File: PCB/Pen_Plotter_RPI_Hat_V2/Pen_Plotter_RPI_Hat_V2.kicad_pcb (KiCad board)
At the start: 4 copper layers, 85 x 56 mm, 33 parts, among them J1 RASM712PX, J2 X_LIMIT_SWITCH, J3 X-AXIS_STEPPER, J4 Y_LIMIT_SWITCH, J5 SERVO, J6 Y-AXIS_STEPPER, J7 PAPER_SENSOR, J8 DC_MOTOR, U1 BIDIRECTIONAL_LEVEL_SHIFTER_7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, U2 MINI560, U3 METRO_MINI_2590, U4 X-AXIS_DRV8825_STEPPER_MOTOR_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, U5 Y-AXIS_DRV8825_STEPPER_MOTOR_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, U6 RPI3-MODBP-BULK, U7 LM393AN

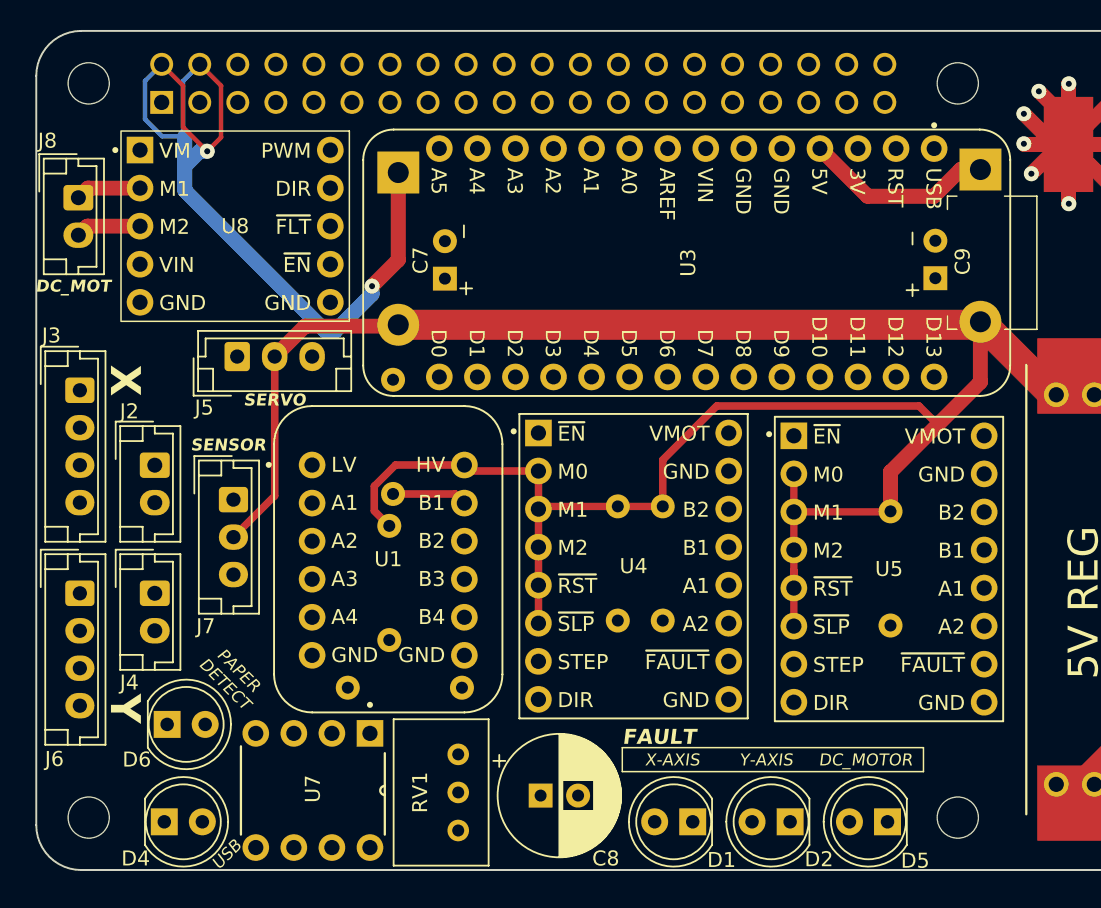
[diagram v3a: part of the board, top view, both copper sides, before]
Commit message: Completed PCB routing, working on resolving final DRC errors
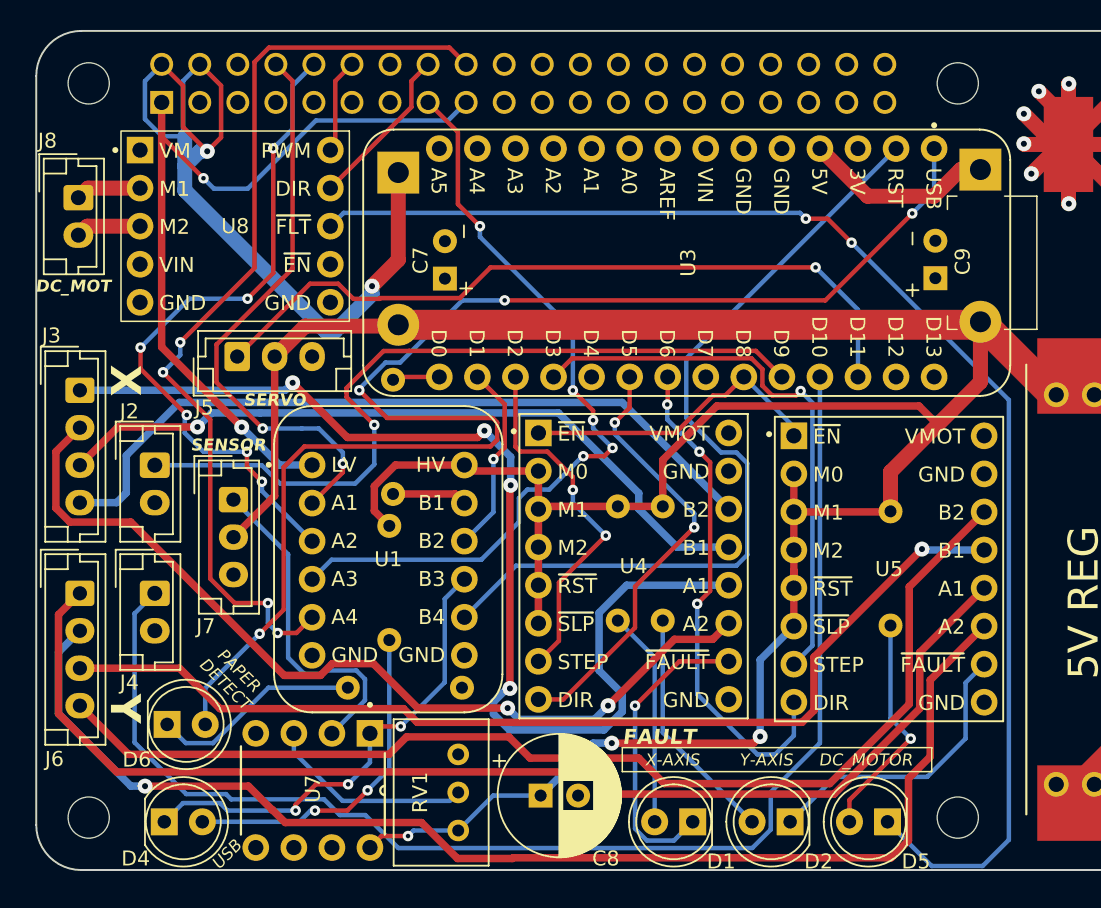
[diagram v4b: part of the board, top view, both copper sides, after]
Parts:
- D1, D2, D5: footprint LED_THT:LED_D5.0mm -> Pen_Plotter_Lib:LED_D5.0mm
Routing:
- net Net-(D6-A): track 0.00 -> 92.4 mm, vias 0 -> 4
- net /Raspberry Pi/DC_MOT_FLT: track 0.00 -> 90.2 mm, vias 0 -> 2
- net Y_LIMIT: track 0.00 -> 88.0 mm
- net /Stepper Motors/Y-AXIS_A2: track 0.00 -> 83.8 mm, vias 0 -> 1
- net /Stepper Motors/Y-AXIS_A1: track 0.00 -> 80.5 mm
- net /Stepper Motors/Y-AXIS_B2: track 0.00 -> 75.6 mm
- net /Stepper Motors/X-AXIS_A1: track 0.00 -> 75.3 mm, vias 0 -> 4
- net /Stepper Motors/Y_AXIS_B1: track 0.00 -> 68.7 mm, vias 0 -> 1
- net MCU_RESET_3V3: track 0.00 -> 62.8 mm, vias 0 -> 4
- net /Stepper Motors/X-AXIS_A2: track 0.00 -> 60.1 mm, vias 0 -> 2
- net +3V3: track 0.00 -> 56.1 mm, vias 0 -> 2
- net MCU_RESET: track 0.00 -> 55.8 mm
- net PAPER_SENSOR_OUT_3V3: track 0.00 -> 52.8 mm, vias 0 -> 5
- net X_LIMIT: track 0.00 -> 52.4 mm, vias 0 -> 1
- net /Stepper Motors/X-AXIS_B2: track 0.00 -> 50.5 mm
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
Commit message: Completed PCB
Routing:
- net /Stepper Motors/Y-AXIS_A2: track 83.8 -> 85.8 mm

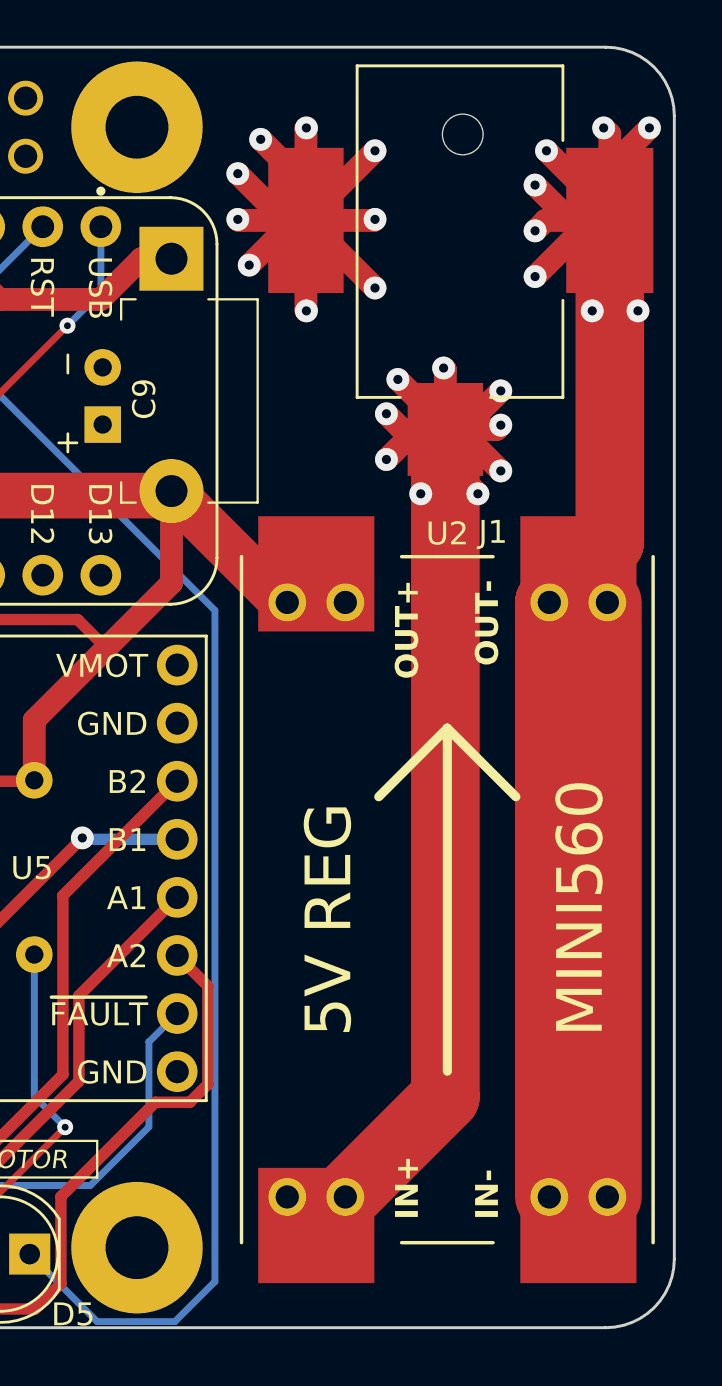
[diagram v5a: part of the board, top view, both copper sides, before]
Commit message: Made PCB use new model for MINI560
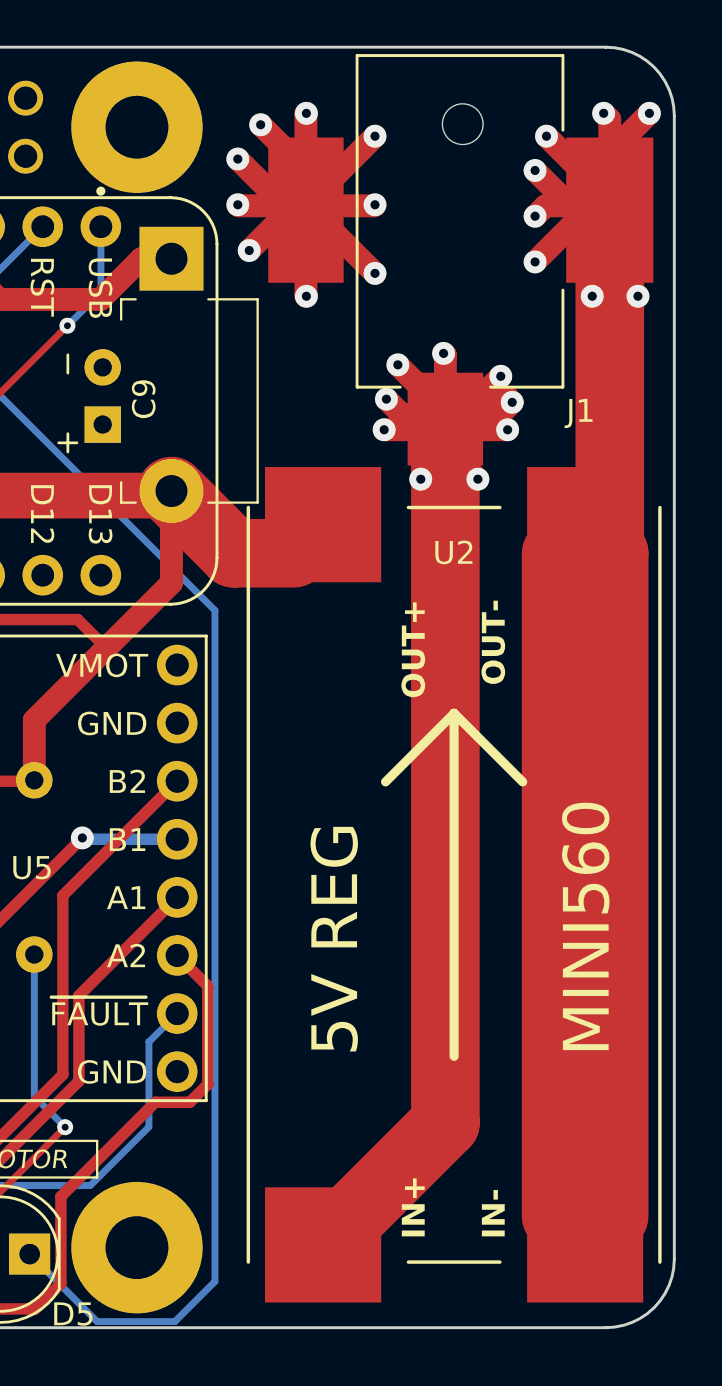
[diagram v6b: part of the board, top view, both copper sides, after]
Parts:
- moved U2 0.90 mm to (140.5, 87.6)
- moved J1 0.45 mm to (131.8, 41.6)
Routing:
- net +12V: track 60.8 -> 65.6 mm
- net GND: track 137.5 -> 140.8 mm
- net +5V: track 195.4 -> 194.8 mm

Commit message: Started work on fixing last few problems
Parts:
- moved D6 6.56 mm to (64.5, 87.3)
- moved D4 6.45 mm to (64.9, 80.8)
- moved U1 1.12 mm to (80.7, 69.7)
- moved R5 1.05 mm to (80.8, 71.5)
- moved U4 1.00 mm to (97.0, 70.2)
- moved R2 0.98 mm to (81.6, 78.5)
- moved R3 0.83 mm to (95.8, 69.8)
- moved R4 0.83 mm to (98.8, 69.8)
- moved R1 0.80 mm to (80.8, 61.6)
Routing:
- net Net-(D6-A): track 92.4 -> 46.8 mm, vias 4 -> 3
- net /Raspberry Pi/PAPER_SENSOR_OUT_LED_POS: track 22.5 -> 0.00 mm, vias 2 -> 0
- net PAPER_SENSOR_OUT_5V: track 31.8 -> 14.3 mm, vias 3 -> 1
- net Net-(D6-K): track 14.1 -> 0.00 mm
- net MCU_TX: track 12.8 -> 23.0 mm, vias 1 -> 0
- net Net-(J7-Pin_1): track 22.5 -> 18.3 mm
- net DIR_X: track 29.4 -> 28.0 mm
- net /Stepper Motors/X_AXIS_B1: track 49.1 -> 50.3 mm
- net +3V3: track 56.1 -> 57.2 mm
- net MCU_RESET_3V3: track 62.8 -> 64.0 mm
- net RPI_RX: track 45.4 -> 46.5 mm
- net /Stepper Motors/X-AXIS_A2: track 60.1 -> 61.2 mm
- net /Stepper Motors/X-AXIS_FLT: track 20.4 -> 21.4 mm
- net /Stepper Motors/X-AXIS_B2: track 50.5 -> 51.5 mm
- net MCU_RESET: track 55.8 -> 56.7 mm
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
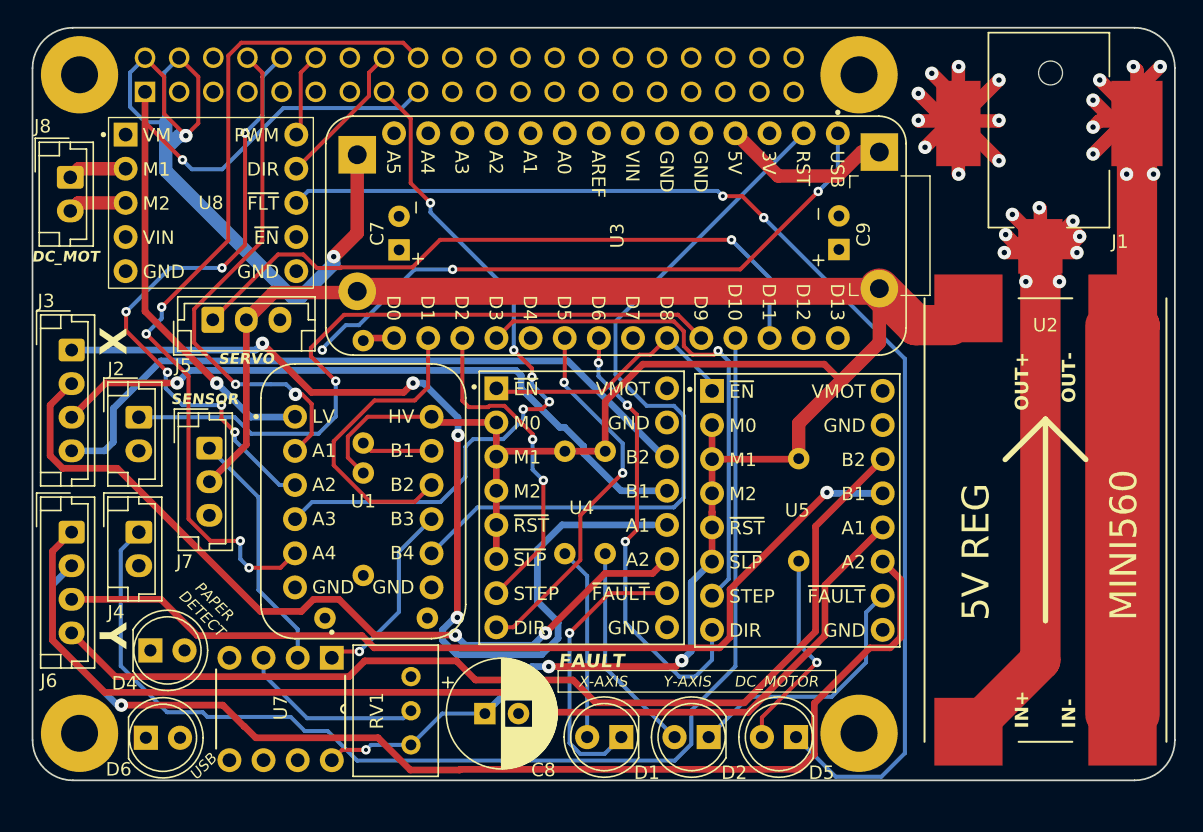
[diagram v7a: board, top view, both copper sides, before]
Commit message: Started work on converting to atmega328p control circuit
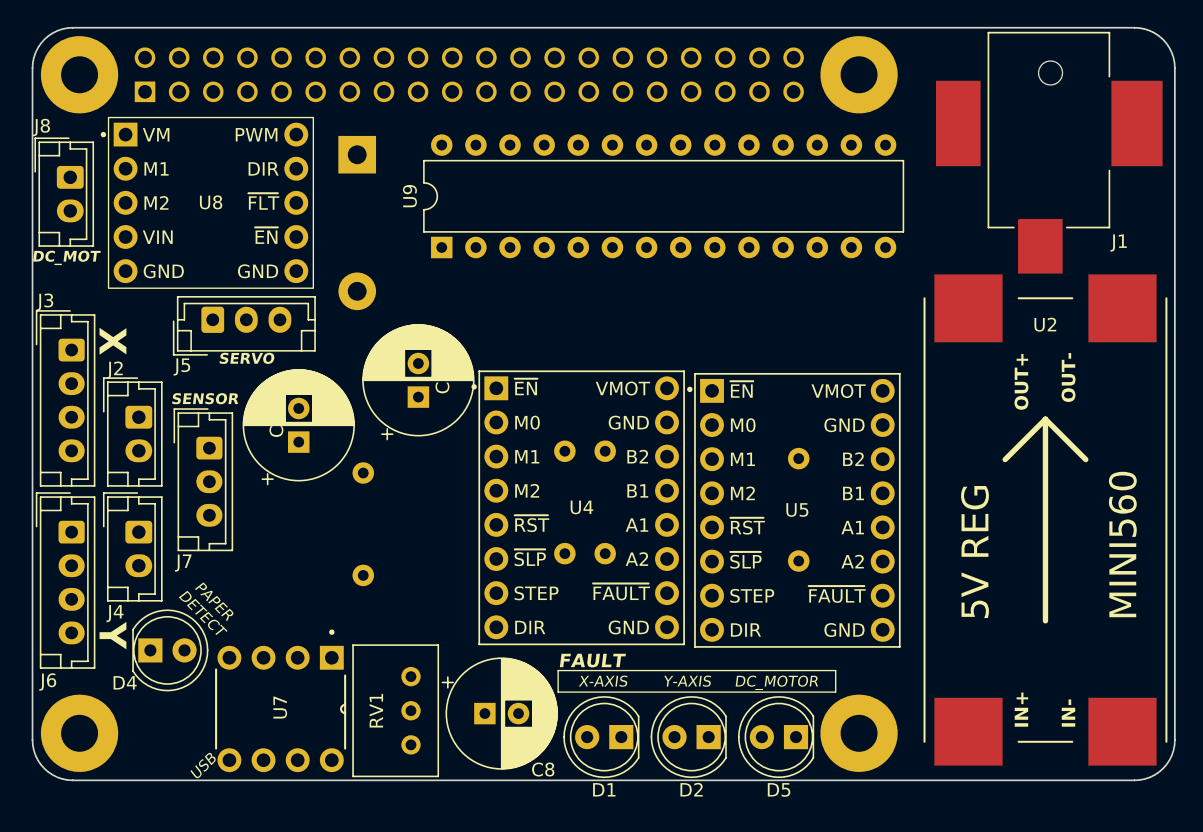
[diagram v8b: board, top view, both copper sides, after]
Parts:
- removed D6: GREEN, LED_THT:LED_D5.0mm
- removed D7: DIODE, Diode_THT:D_5W_P10.16mm_Horizontal
- removed R1, R2: 10k, Pen_Plotter_Lib:THT_RESISTOR_WITH_VALUE
- removed U1: BIDIRECTIONAL_LEVEL_SHIFTER_757, Pen_Plotter_Lib:BIDIRECTIONAL_LEVEL_SHIFTER_575
- removed U3: METRO_MINI_2590, Pen_Plotter_Lib:METRO_MINI_MODULE_2590
- added U9: ATmega328P-P, Package_DIP:DIP-28_W7.62mm, F.Cu at (86.5, 50.8)
- D1, D2, D5: footprint Pen_Plotter_Lib:LED_D5.0mm -> LED_THT:LED_D5.0mm
- moved C9 33.2 mm to (84.8, 62.0)
- moved C7 16.1 mm to (75.9, 65.3)
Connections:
- D4 pad 1: PAPER_SENSOR_OUT_5V -> PAPER_SENSOR_OUT_3V3
- R5 pad 1: +5V -> +3V3
- U6 pad 10: RPI_RX -> MCU_TX
- U6 pad 18: MCU_RESET_3V3 -> MCU_RESET
- U6 pad 32: unconnected-(U6-GPIO12-Pad32) -> MCU_ABORT
- U6 pad 33: unconnected-(U6-GPIO13-Pad33) -> MCU_HOLD
- U6 pad 36: unconnected-(U6-GPIO16-Pad36) -> MCU_RESUME
- U6 pad 8: RPI_TX -> MCU_RX
- U7 pad 1: PAPER_SENSOR_OUT_5V -> PAPER_SENSOR_OUT_3V3
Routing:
- net +5V: track 194.4 -> 0.00 mm, vias 3 -> 0
- net GND: track 140.8 -> 0.00 mm, vias 17 -> 0
- net /Raspberry Pi/DC_MOT_FLT: track 90.2 -> 0.00 mm, vias 2 -> 0
- net Y_LIMIT: track 88.0 -> 0.00 mm
- net /Stepper Motors/Y-AXIS_A2: track 85.8 -> 0.00 mm, vias 1 -> 0
- net /Stepper Motors/Y-AXIS_A1: track 80.5 -> 0.00 mm
- net /Stepper Motors/Y-AXIS_B2: track 75.6 -> 0.00 mm
- net /Stepper Motors/X-AXIS_A1: track 75.2 -> 0.00 mm, vias 4 -> 0
- net /Stepper Motors/Y_AXIS_B1: track 68.7 -> 0.00 mm, vias 1 -> 0
- net +12V: track 65.6 -> 0.00 mm, vias 9 -> 0
- net MCU_RESET_3V3: track 64.0 -> 0.00 mm, vias 4 -> 0
- net /Stepper Motors/X-AXIS_A2: track 61.2 -> 0.00 mm, vias 2 -> 0
- net Net-(D3-K): track 58.2 -> 0.00 mm, vias 2 -> 0
- net +3V3: track 57.2 -> 0.00 mm, vias 2 -> 0
- net MCU_RESET: track 56.7 -> 0.00 mm
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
